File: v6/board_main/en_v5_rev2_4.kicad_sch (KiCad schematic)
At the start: 35 parts, among them U6 W25Q16JVUXIQ, U7 RP2040, X1 12MHz

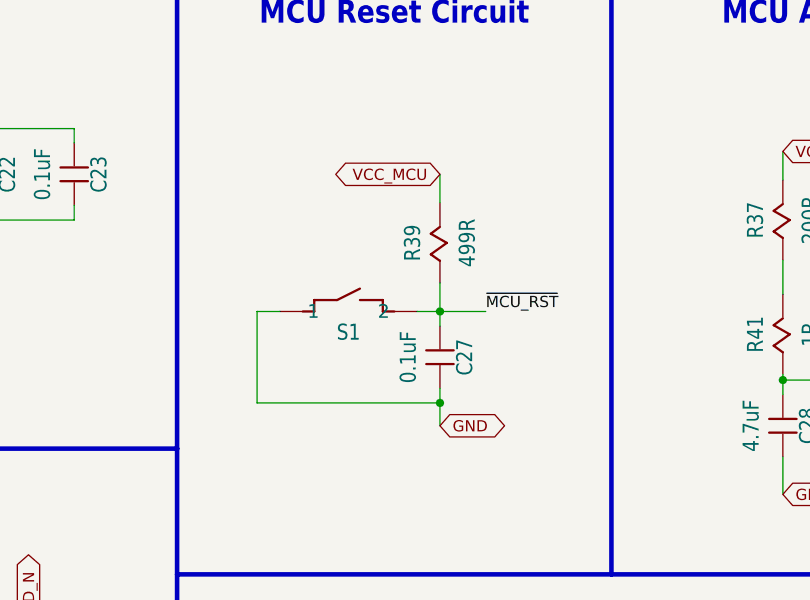
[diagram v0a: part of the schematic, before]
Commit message: Rephrasing ENV5 design
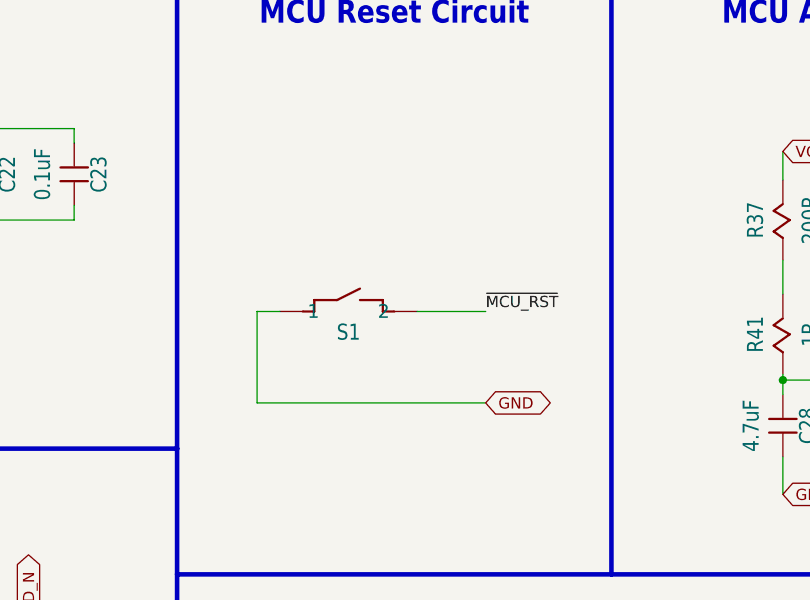
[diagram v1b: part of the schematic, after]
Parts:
- removed C27: 0.1uF, env:0402, symbol env-eagle-import:CAPACITOR0402
- removed R39: 499R, env:0402, symbol env-eagle-import:RESISTORSMD_0402
